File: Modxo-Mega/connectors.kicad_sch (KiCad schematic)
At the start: 6 parts, among them J3 LCD, J4 UART, J5 D0, J6 OXHD, J7 RGB, J9 EXP I2C

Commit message: Cleanup schematic
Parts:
- renumbered J9 to J8
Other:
- moved on the sheet: J3, J4, J5, J6, J7, J8

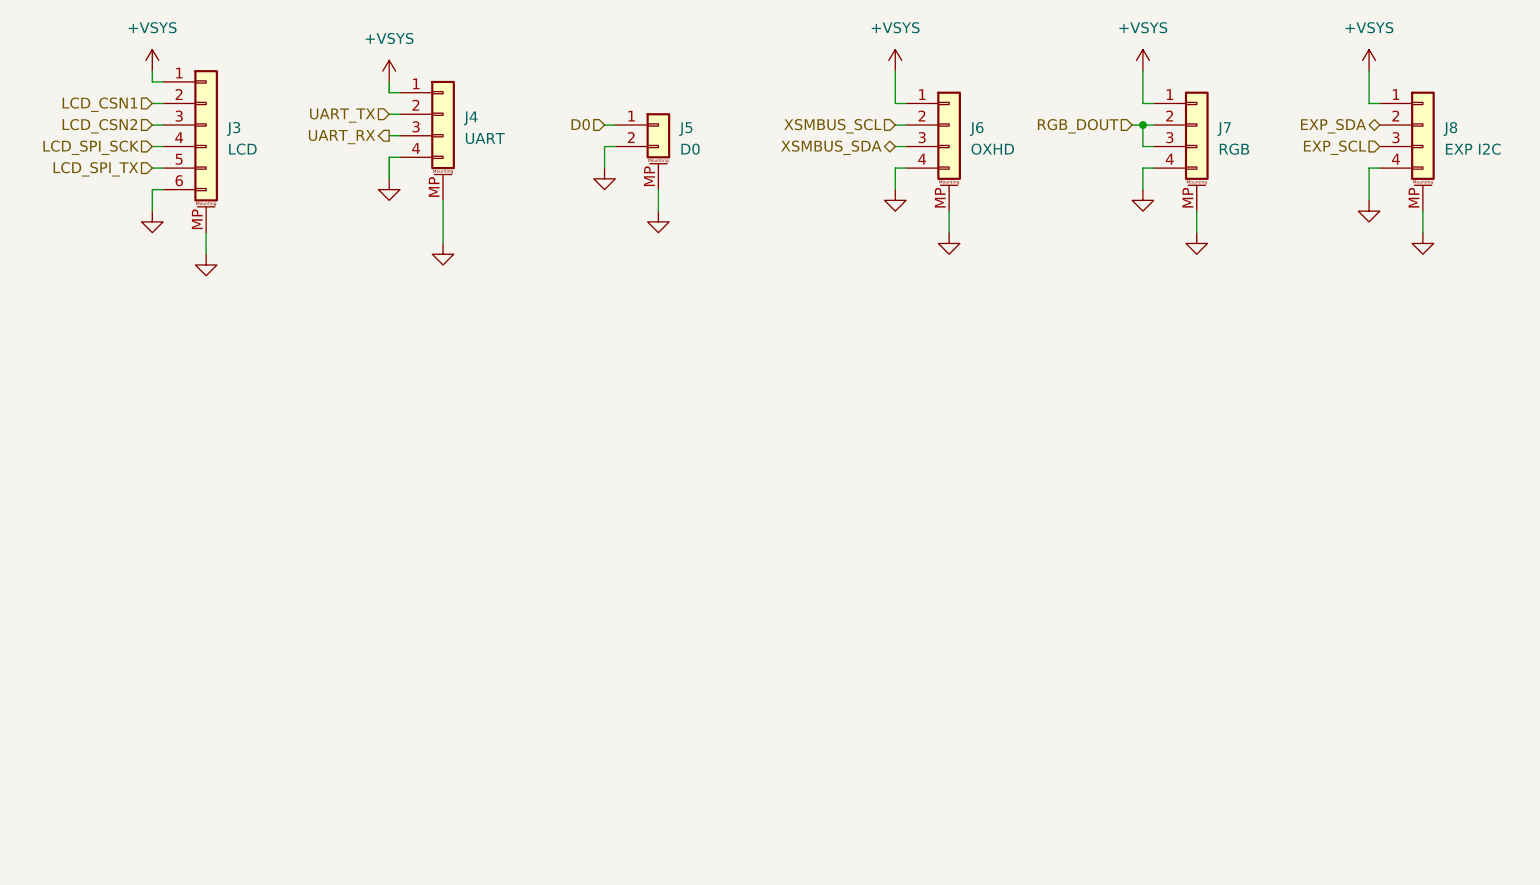
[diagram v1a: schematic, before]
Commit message: Add SD Card, other minor changes
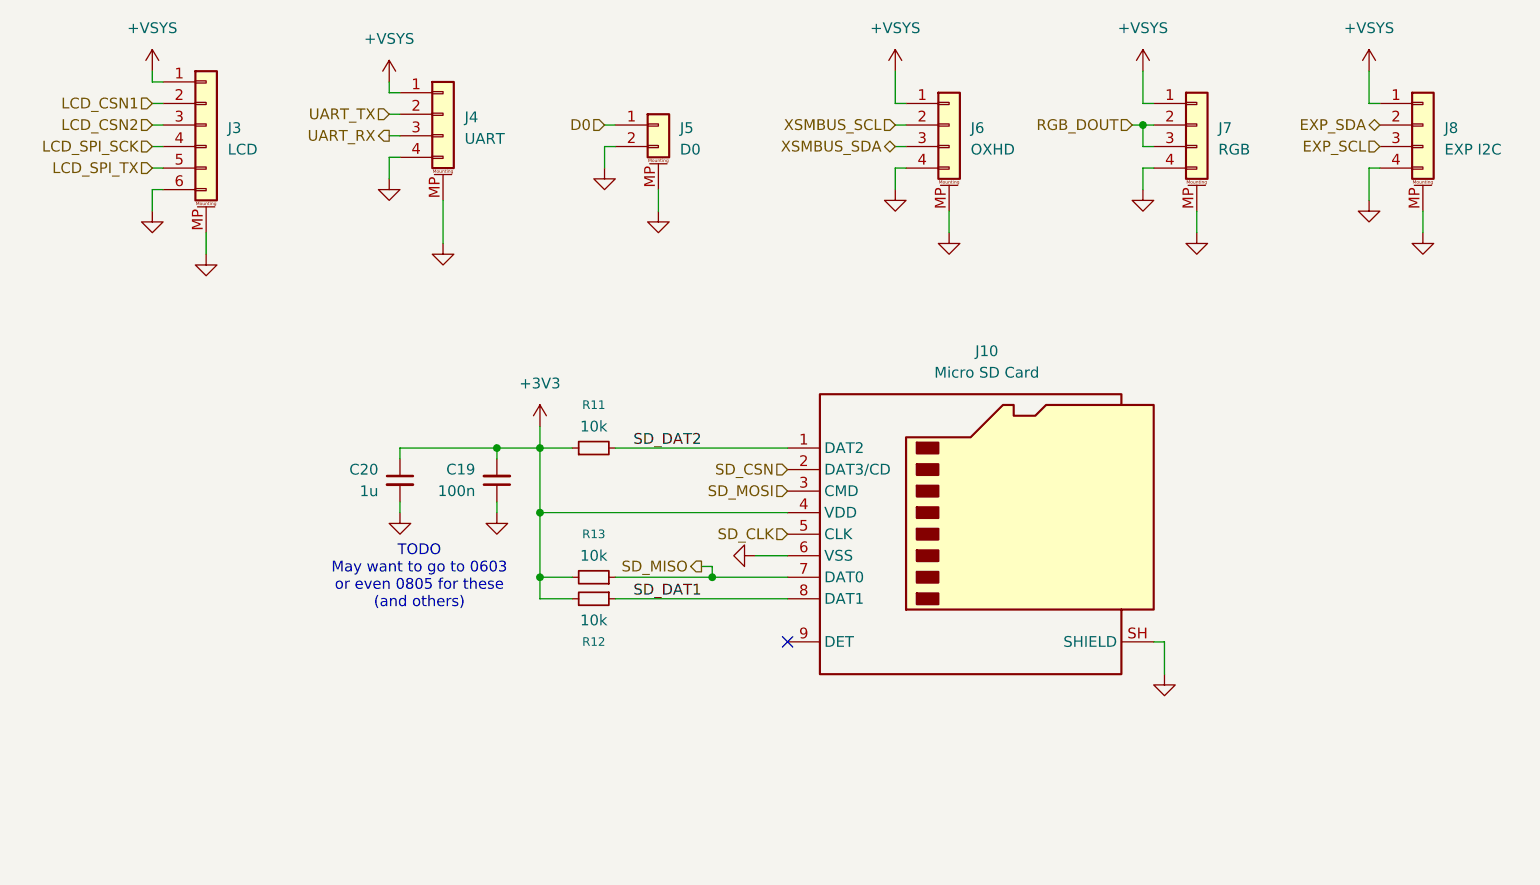
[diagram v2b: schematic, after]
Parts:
- added C19: 100n, Capacitor_SMD:C_0402_1005Metric, symbol Modxo-Designs:C_100n_0402_Decouple
- added C20: 1u, Capacitor_SMD:C_0402_1005Metric, symbol Modxo-Designs:C_1u_0402_Decouple
- added J10: Micro SD Card, Modxo-Designs:MSD-1-A, symbol Connector:Micro_SD_Card_Det1
- added R11, R12, R13: 10k, Resistor_SMD:R_0603_1608Metric, symbol Modxo-Designs:R_10k_0603_PullUp
- J4, J7, J8: symbol Connector_Generic_MountingPin:Conn_01x04_MountingPin -> Modxo-Designs:Conn_01x04_JST_SH
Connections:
- net GND: now also C19.1, C20.2, J10.6 (VSS), J10.SH (SHIELD)
- new net +3V3: C19.2, C20.1, J10.4 (VDD), R11.1, R12.2, R13.2
- new net SD_CLK: J10.5 (CLK)
- new net SD_CSN: J10.2 (DAT3/CD)
- new net SD_DAT1: J10.8 (DAT1), R12.1
- new net SD_DAT2: J10.1 (DAT2), R11.2
- new net SD_MISO: J10.7 (DAT0), R13.1
- new net SD_MOSI: J10.3 (CMD)
- no-connect marks 0 -> 1
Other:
- note added: "TODO May want to go to 0603 or even 0805 for these (and others)"

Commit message: Move most symbols to library
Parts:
- C20: footprint Capacitor_SMD:C_0402_1005Metric -> Capacitor_SMD:C_0603_1608Metric; symbol Modxo-Designs:C_1u_0402_Decouple -> Modxo-Designs:C_1u_0603_Decouple; Distributor Link 1 https://www.digikey.com/en/products/detail/samsung-electro-mechanics/CL05A105KA5NQNC/3887103?s=N4IgTCBcDaIMIBkAMBWAggRlQaTSgcgIr5wgC6AvkA -> https://www.digikey.com/en/products/detail/samsung-electro-mechanics/CL10A105KB8NNNC/3887518; Distributor Link 2 https://www.mouser.com/ProductDetail/Samsung-Electro-Mechan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 -> https://www.mouser.com/en/ProductDetail/Samsung-Electro-Mec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; LCSC C52923 -> C1592; Manufacturer Part Number CL05A105KA5NQNC -> CL10A105KO8NNNC
- J10: symbol Connector:Micro_SD_Card_Det1 -> Modxo-Designs:Micro_SD_Card_Slot
- J3: symbol Connector_Generic_MountingPin:Conn_01x06_MountingPin -> Modxo-Designs:Conn_01x06_JST_SH
- J5: symbol Connector_Generic_MountingPin:Conn_01x02_MountingPin -> Modxo-Designs:Conn_01x02_JST_SH
- J6: symbol Connector_Generic_MountingPin:Conn_01x04_MountingPin -> Modxo-Designs:Conn_01x04_PicoBlade
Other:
- note removed: "TODO May want to go to 0603 or even 0805 for these (and others)"
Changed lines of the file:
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@@
 	(generator_version "10.0")
 	(paper "A4")
-	(text "TODO\nMay want to go to 0603\nor even 0805 for these\n(and others)"
-		(exclude_from_sim no)
-		(at 87.376 92.71 0)
-		(effects
-			(font
-				(size 1.27 1.27)
-			)
-		)
-	)
 	(junction
 		(at 101.6 77.47)
@@
 	)
 	(symbol
-		(lib_id "Connector_Generic_MountingPin:Conn_01x02_MountingPin")
+		(lib_id "Modxo-Designs:Conn_01x02_JST_SH")
 		(at 115.57 39.37 0)
 		(unit 1)
@@
 	)
 	(symbol
-		(lib_id "Connector_Generic_MountingPin:Conn_01x04_MountingPin")
+		(lib_id "Modxo-Designs:Conn_01x04_PicoBlade")
 		(at 149.86 39.37 0)
 		(unit 1)
@@
 	)
 	(symbol
-		(lib_id "Modxo-Designs:C_1u_0402_Decouple")
+		(lib_id "Modxo-Designs:C_1u_0603_Decouple")
 		(at 85.09 81.28 0)
 		(unit 1)
@@
 			)
 		)
-		(property "Footprint" "Capacitor_SMD:C_0402_1005Metric"
+		(property "Footprint" "Capacitor_SMD:C_0603_1608Metric"
 			(at 85.09 81.28 0)
 			(hide yes)
@@
 			)
 		)
-		(property "Datasheet" "https://mm.digikey.com/Volume0/opasdata/d220001/medias/docus/41/CL05A105KA5NQNC.pdf"
+		(property "Datasheet" "kicad-embed://02336ea48ea44ca18c72517dd3cb7b47.pdf"
 			(at 85.09 81.28 0)
 			(hide yes)
@@
 			)
 		)
-		(property "Description" "1uF ±10% 25V Ceramic Capacitor X5R 0402"
+		(property "Description" "1uF ±10% 16V Ceramic Capacitor X5R 0603"
 			(at 85.09 81.28 0)
 			(hide yes)
@@
 			)
 		)
-		(property "Manufacturer Part Number" "CL05A105KA5NQNC"
+		(property "Manufacturer Part Number" "CL10A105KO8NNNC"
 			(at 85.09 81.28 0)
 			(hide yes)
@@
 			)
 		)
-		(property "Distributor Link 1" "https://www.digikey.com/en/products/detail/samsung-electro-mechanics/CL05A105KA5NQNC/3887103?s=N4IgTCBcDaIMIBkAMBWAggRlQaTSgcgIr5wgC6AvkA"
+		(property "Distributor Link 1" "https://www.digikey.com/en/products/detail/samsung-electro-mechanics/CL10A105KB8NNNC/3887518"
 			(at 85.09 81.28 0)
 			(hide yes)
@@
 			)
 		)
-		(property "Distributor Link 2" "https://www.mouser.com/ProductDetail/Samsung-Electro-Mechanics/CL05A105KA5NQNC?qs=X6jEic%2FHinDIeFgZnm60Lw%3D%3D"
+		(property "Distributor Link 2" "https://www.mouser.com/en/ProductDetail/Samsung-Electro-Mechanics/CL10A105KB8NNNC?qs=ktYoCbbtCSJz4pFCLWXd5g%3D%3D"
 			(at 85.09 81.28 0)
 			(hide yes)
@@
 			)
 		)
-		(property "LCSC" "C52923"
+		(property "LCSC" "C1592"
 			(at 85.09 81.28 0)
 			(hide yes)
@@
 	)
 	(symbol
-		(lib_id "Connector:Micro_SD_Card_Det1")
+		(lib_id "Modxo-Designs:Micro_SD_Card_Slot")
 		(at 153.67 87.63 0)
 		(unit 1)
@@
 	)
 	(symbol
-		(lib_id "Connector_Generic_MountingPin:Conn_01x06_MountingPin")
+		(lib_id "Modxo-Designs:Conn_01x06_JST_SH")
 		(at 62.23 39.37 0)
 		(unit 1)
